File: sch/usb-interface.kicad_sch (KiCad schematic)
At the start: 8 parts, among them IC1 USB2244I-AEZG-06

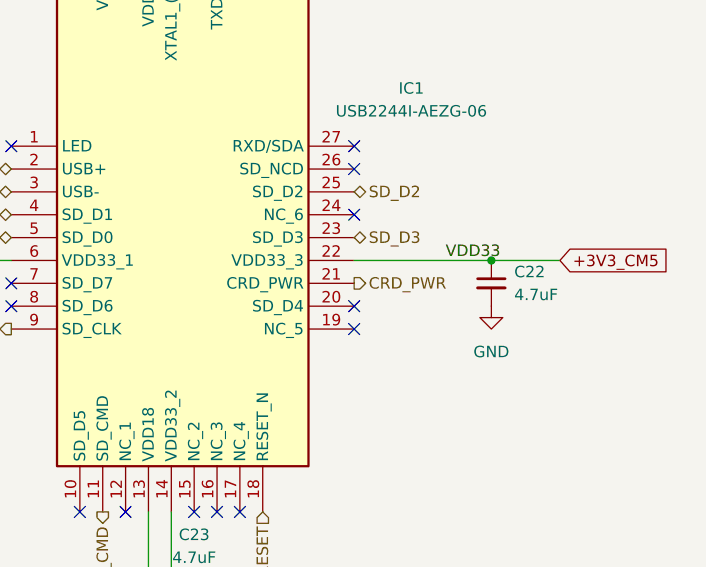
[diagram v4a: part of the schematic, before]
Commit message: changed sd lines impedanc etc. power plane zone 3.3v
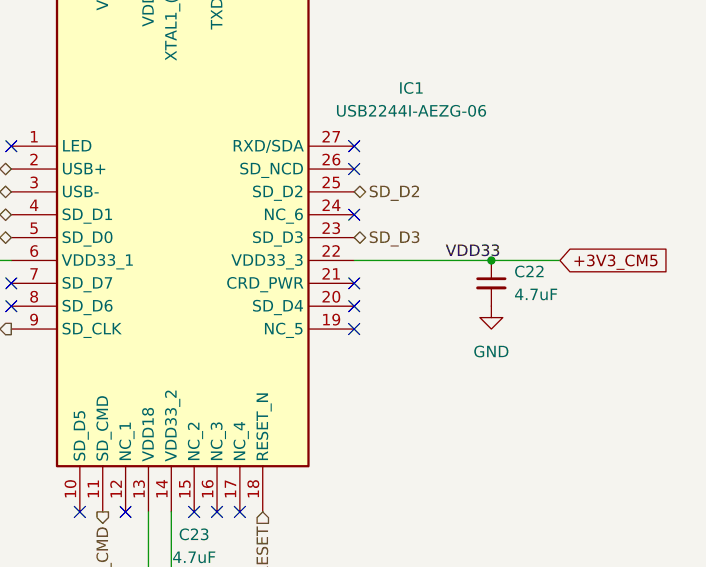
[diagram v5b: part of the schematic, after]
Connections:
- net CRD_PWR: no longer names the net of IC1.21 (CRD_PWR)
- no-connect marks 17 -> 18
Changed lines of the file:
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@@
+	)
+	(no_connect
+		(at 106.68 100.33)
 	)
 	(no_connect
@@
 		)
 	)
-	(hierarchical_label "CRD_PWR"
-		(shape output)
-		(at 106.68 100.33 0)
-		(effects
-			(font
-				(size 1.27 1.27)
-			)
-			(justify left)
-		)
-	)

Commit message: update licence to CERN-OHL-S
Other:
- title: USB Interface -> Audiograb
